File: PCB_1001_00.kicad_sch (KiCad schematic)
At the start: 4 parts, among them SW1 SW_MEC_5G

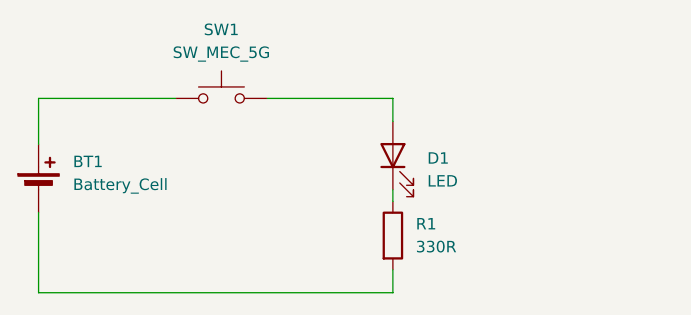
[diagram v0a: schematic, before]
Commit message: VAR_PCA_1001_00 with LED set to DNP
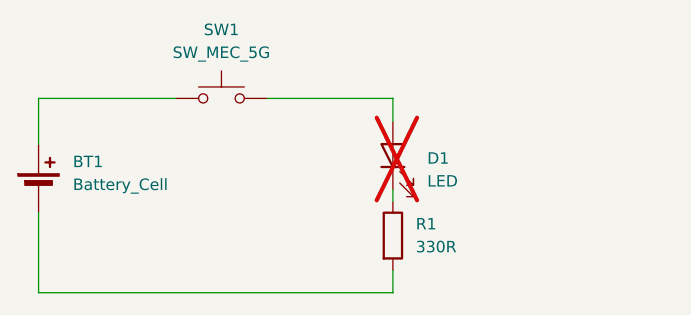
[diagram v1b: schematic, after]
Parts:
- D1: now not fitted
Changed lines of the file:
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@@
 		(in_bom yes)
 		(on_board yes)
-		(dnp no)
+		(dnp yes)
 		(fields_autoplaced yes)
 		(property "Reference" "D1"

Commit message: LED set back to Populate
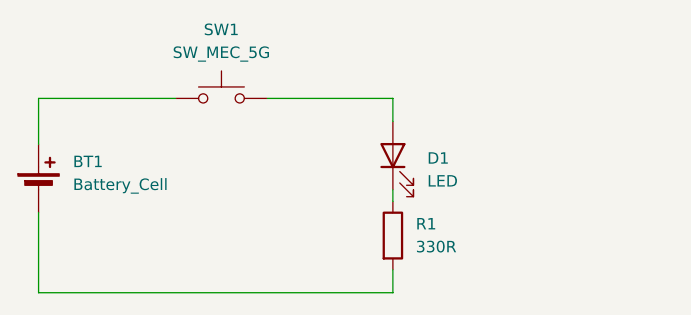
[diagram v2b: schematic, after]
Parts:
- D1: now fitted
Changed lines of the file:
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@@
 		(in_bom yes)
 		(on_board yes)
-		(dnp yes)
+		(dnp no)
 		(fields_autoplaced yes)
 		(property "Reference" "D1"

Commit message: PCB -->01, 2 additional LED circuits
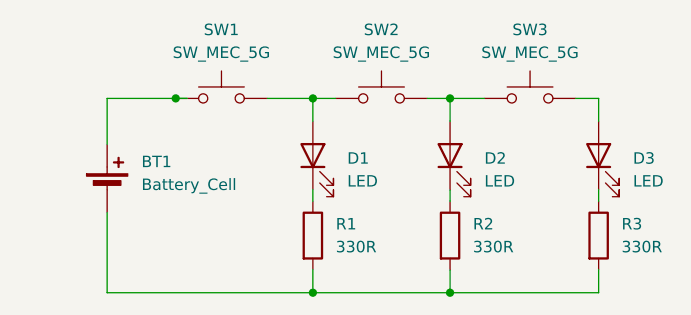
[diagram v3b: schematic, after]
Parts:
- added D2, D3: LED, LED_SMD:LED_0603_1608Metric, symbol Device:LED
- added R2, R3: 330R, Resistor_SMD:R_0603_1608Metric, symbol Device:R
- added SW2, SW3: SW_MEC_5G, Button_Switch_SMD:SW_Tactile_SPST_NO_Straight_CK_PTS636Sx25SMTRLFS, symbol Switch:SW_MEC_5G
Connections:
- net at BT1.2 (-), R1.2: now also R2.2, R3.2
- net at D1.2 (A), SW1.3 (B), SW1.4 (B): now also SW2.1 (A), SW2.2 (A)
- new net: D3.1 (K), R3.1
- new net: D3.2 (A), SW3.3 (B), SW3.4 (B)
- new net: D2.2 (A), SW2.3 (B), SW2.4 (B), SW3.1 (A), SW3.2 (A)
- new net: D2.1 (K), R2.1
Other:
- moved on the sheet: BT1, D1, R1

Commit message: PCB_1001_01 routing completed
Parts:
- removed SW1, SW2, SW3: SW_MEC_5G, Button_Switch_SMD:SW_Tactile_SPST_NO_Straight_CK_PTS636Sx25SMTRLFS, symbol Switch:SW_MEC_5G
- added SW1, SW2, SW3: SW_MEC_5G_edit, Button_Switch_SMD:SW_Tactile_SPST_NO_Straight_CK_PTS636Sx25SMTRLFS, symbol Sym_Library:SW_MEC_5G_edit
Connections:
- net at D3.2 (A): now also SW3.2 (B)
- net at D1.2 (A): now also SW1.2 (B), SW2.1 (A)
- net at D2.2 (A): now also SW2.2 (B), SW3.1 (A)
- net at BT1.1 (+): now also SW1.1 (A)
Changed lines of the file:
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@@
 	(paper "A4")
-	(junction
-		(at 135.89 88.9)
-		(diameter 0)
-		(color 0 0 0 0)
-	)
 	(junction
 		(at 151.13 110.49)
@@
 	(wire
 		(pts
+			(xy 128.27 88.9) (xy 135.89 88.9)
+		)
+		(stroke
+			(width 0)
+			(type default)
+		)
+	)
+	(wire
+		(pts
 			(xy 163.83 88.9) (xy 166.37 88.9)
 		)
@@
 	(wire
 		(pts
-			(xy 137.16 88.9) (xy 135.89 88.9)
-		)
-		(stroke
-			(width 0)
-			(type default)
-		)
-	)
-	(wire
-		(pts
 			(xy 128.27 88.9) (xy 128.27 93.98)
 		)
@@
 	(wire
 		(pts
-			(xy 135.89 88.9) (xy 128.27 88.9)
-		)
-		(stroke
-			(width 0)
-			(type default)
-		)
-	)
-	(wire
-		(pts
 			(xy 182.88 88.9) (xy 182.88 91.44)
 		)
@@
 			(width 0)
 			(type default)
+		)
+	)
+	(symbol
+		(lib_id "Sym_Library:SW_MEC_5G_edit")
+		(at 175.26 88.9 0)
+		(unit 1)
+		(exclude_from_sim no)
+		(in_bom yes)
+		(on_board yes)
+		(dnp no)
+		(fields_autoplaced yes)
+		(property "Reference" "SW3"
+			(at 175.26 81.28 0)
+			(effects
+				(font
+					(size 1.27 1.27)
+				)
+			)
+		)
+		(property "Value" "SW_MEC_5G_edit"
+			(at 175.26 83.82 0)
+			(effects
+				(font
+					(size 1.27 1.27)
+				)
+			)
+		)
+		(property "Footprint" "Button_Switch_SMD:SW_Tactile_SPST_NO_Straight_CK_PTS636Sx25SMTRLFS"
+			(at 175.26 83.82 0)
+			(effects
+				(font
+					(size 1.27 1.27)
+				)
+				(hide yes)
+			)
+		)
+		(property "Datasheet" "http://www.apem.com/int/index.php?controller=attachment&id_attachment=488"
+			(at 175.26 83.82 0)
+			(effects
+				(font
+					(size 1.27 1.27)
+				)
+				(hide yes)
+			)
+		)
+		(property "Description" "MEC 5G single pole normally-open tactile switch"
+			(at 175.26 88.9 0)
+			(effects
+				(font
+					(size 1.27 1.27)
+				)
+				(hide yes)
+			)
+		)
+		(pin "1"
+		)
+		(pin "2"
+		)
+		(instances
+			(project ""
+				(path "/9c4608c9-b9d4-4f6a-9cb6-835175086c03"
+					(reference "SW3")
+					(unit 1)
+				)
+			)
+		)
+	)
+	(symbol
+		(lib_id "Sym_Library:SW_MEC_5G_edit")
+		(at 140.97 88.9 0)
+		(unit 1)
+		(exclude_from_sim no)
+		(in_bom yes)
+		(on_board yes)
+		(dnp no)
+		(fields_autoplaced yes)
+		(property "Reference" "SW1"
+			(at 140.97 81.28 0)
+			(effects
+				(font
+					(size 1.27 1.27)
+				)
+			)
+		)
+		(property "Value" "SW_MEC_5G_edit"
+			(at 140.97 83.82 0)
+			(effects
+				(font
+					(size 1.27 1.27)
+				)
+			)
+		)
+		(property "Footprint" "Button_Switch_SMD:SW_Tactile_SPST_NO_Straight_CK_PTS636Sx25SMTRLFS"
+			(at 140.97 83.82 0)
+			(effects
+				(font
+					(size 1.27 1.27)
+				)
+				(hide yes)
+			)
+		)
+		(property "Datasheet" "http://www.apem.com/int/index.php?controller=attachment&id_attachment=488"
+			(at 140.97 83.82 0)
+			(effects
+				(font
+					(size 1.27 1.27)
+				)
+				(hide yes)
+			)
+		)
+		(property "Description" "MEC 5G single pole normally-open tactile switch"
+			(at 140.97 88.9 0)
+			(effects
+				(font
+					(size 1.27 1.27)
+				)
+				(hide yes)
+			)
+		)
+		(pin "2"
+		)
+		(pin "1"
+		)
+		(instances
+			(project ""
+				(path "/9c4608c9-b9d4-4f6a-9cb6-835175086c03"
+					(reference "SW1")
+					(unit 1)
+				)
+			)
 		)
 	)
@@
 	)
 	(symbol
-		(lib_id "Switch:SW_MEC_5G")
+		(lib_id "Sym_Library:SW_MEC_5G_edit")
 		(at 158.75 88.9 0)
 		(unit 1)
@@
 			)
 		)
-		(property "Value" "SW_MEC_5G"
+		(property "Value" "SW_MEC_5G_edit"
 			(at 158.75 83.82 0)
 			(effects
@@
 			)
 		)
-		(pin "3"
-		)
-		(pin "2"
-		)
-		(pin "1"
-		)
-		(pin "4"
-		)
-		(instances
-			(project "PCB_1001_00"
+		(pin "1"
+		)
+		(pin "2"
+		)
+		(instances
+			(project ""
 				(path "/9c4608c9-b9d4-4f6a-9cb6-835175086c03"
 					(reference "SW2")
-					(unit 1)
-				)
-			)
-		)
-	)
-	(symbol
-		(lib_id "Switch:SW_MEC_5G")
-		(at 140.97 88.9 0)
-		(unit 1)
-		(exclude_from_sim no)
-		(in_bom yes)
-		(on_board yes)
-		(dnp no)
-		(fields_autoplaced yes)
-		(property "Reference" "SW1"
-			(at 140.97 81.28 0)
-			(effects
-				(font
-					(size 1.27 1.27)
-				)
-			)
-		)
-		(property "Value" "SW_MEC_5G"
-			(at 140.97 83.82 0)
-			(effects
-				(font
-					(size 1.27 1.27)
-				)
-			)
-		)
-		(property "Footprint" "Button_Switch_SMD:SW_Tactile_SPST_NO_Straight_CK_PTS636Sx25SMTRLFS"
-			(at 140.97 83.82 0)
-			(effects
-				(font
-					(size 1.27 1.27)
-				)
-				(hide yes)
-			)
-		)
-		(property "Datasheet" "http://www.apem.com/int/index.php?controller=attachment&id_attachment=488"
-			(at 140.97 83.82 0)
-			(effects
-				(font
-					(size 1.27 1.27)
-				)
-				(hide yes)
-			)
-		)
-		(property "Description" "MEC 5G single pole normally-open tactile switch"
-			(at 140.97 88.9 0)
-			(effects
-				(font
-					(size 1.27 1.27)
-				)
-				(hide yes)
-			)
-		)
-		(pin "3"
-		)
-		(pin "2"
-		)
-		(pin "1"
-		)
-		(pin "4"
-		)
-		(instances
-			(project ""
-				(path "/9c4608c9-b9d4-4f6a-9cb6-835175086c03"
-					(reference "SW1")
 					(unit 1)
 				)
@@
 					(unit 1)
 				)
-			)
-		)
-	)
-	(symbol
-		(lib_id "Switch:SW_MEC_5G")
-		(at 175.26 88.9 0)
-		(unit 1)
-		(exclude_from_sim no)
-		(in_bom yes)
-		(on_board yes)
-		(dnp no)
-		(fields_autoplaced yes)
-		(property "Reference" "SW3"
-			(at 175.26 81.28 0)
-			(effects
-				(font
-					(size 1.27 1.27)
-				)
-			)
-		)
-		(property "Value" "SW_MEC_5G"
-			(at 175.26 83.82 0)
-			(effects
-				(font
-					(size 1.27 1.27)
-				)
-			)
-		)
-		(property "Footprint" "Button_Switch_SMD:SW_Tactile_SPST_NO_Straight_CK_PTS636Sx25SMTRLFS"
-			(at 175.26 83.82 0)
-			(effects
-				(font
-					(size 1.27 1.27)
-				)
-				(hide yes)
-			)
-		)
-		(property "Datasheet" "http://www.apem.com/int/index.php?controller=attachment&id_attachment=488"
-			(at 175.26 83.82 0)
-			(effects
-				(font
-					(size 1.27 1.27)
-				)
-				(hide yes)
-			)
-		)
-		(property "Description" "MEC 5G single pole normally-open tactile switch"
-			(at 175.26 88.9 0)
-			(effects
-				(font
-					(size 1.27 1.27)
-				)
-				(hide yes)
-			)
-		)
-		(pin "3"
-		)
-		(pin "2"
-		)
-		(pin "1"
-		)
-		(pin "4"
-		)
-		(instances
-			(project "PCB_1001_00"
-				(path "/9c4608c9-b9d4-4f6a-9cb6-835175086c03"
-					(reference "SW3")
-					(unit 1)
-				)

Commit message: Gerbers, Schematic and BOM outputs created
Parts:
- D3, R3, SW3: now not fitted
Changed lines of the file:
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@@
 		(in_bom yes)
 		(on_board yes)
-		(dnp no)
+		(dnp yes)
 		(fields_autoplaced yes)
 		(property "Reference" "SW3"
@@
 		(in_bom yes)
 		(on_board yes)
-		(dnp no)
+		(dnp yes)
 		(fields_autoplaced yes)
 		(property "Reference" "R3"
@@
 		(in_bom yes)
 		(on_board yes)
-		(dnp no)
+		(dnp yes)
 		(fields_autoplaced yes)
 		(property "Reference" "D3"

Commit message: PCA_1003_00 Initial Commit
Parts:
- D2, R2, SW2: now not fitted
- D3, R3, SW3: now fitted
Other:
- title: (none) -> PCA_1003_00
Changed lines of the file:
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@@
 	(generator_version "8.0")
 	(paper "A4")
+	(title_block
+		(title "PCA_1003_00")
+		(date "2025-04-01")
+		(rev "00")
+	)
 	(junction
 		(at 151.13 110.49)
@@
 		(in_bom yes)
 		(on_board yes)
-		(dnp yes)
+		(dnp no)
 		(fields_autoplaced yes)
 		(property "Reference" "SW3"
@@
 		(in_bom yes)
 		(on_board yes)
-		(dnp yes)
+		(dnp no)
 		(fields_autoplaced yes)
 		(property "Reference" "R3"
@@
 		(in_bom yes)
 		(on_board yes)
-		(dnp yes)
+		(dnp no)
 		(fields_autoplaced yes)
 		(property "Reference" "D3"
@@
 		(in_bom yes)
 		(on_board yes)
-		(dnp no)
+		(dnp yes)
 		(fields_autoplaced yes)
 		(property "Reference" "SW2"
@@
 		(in_bom yes)
 		(on_board yes)
-		(dnp no)
+		(dnp yes)
 		(fields_autoplaced yes)
 		(property "Reference" "R2"
@@
 		(in_bom yes)
 		(on_board yes)
-		(dnp no)
+		(dnp yes)
 		(fields_autoplaced yes)
 		(property "Reference" "D2"
